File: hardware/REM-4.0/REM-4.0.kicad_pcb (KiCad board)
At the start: 2 copper layers, 98.4 x 44.5 mm, 35 parts, among them J1 Conn_01x04, J2 Conn_01x03, Q1 IRF840, U1 NE555P

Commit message: new file:   .~BoM.xlsx 	new file:   BoM.xlsx 	new file:   hardware/BoM.xlsx 	deleted:    hardware/MSD-1.0/MSD-1.0-backups/MSD-1.0-2025-03-26_092035.zip 	deleted:    hardware/MSD-1.0/MSD-1.0-backups/MSD-1.0-2025-03-26_092834.zip 	deleted:    hardware/MSD-1.0/MSD-1.0-backups/MSD-1.0-2025-03-27_092014.zip 	new file:   hardware/MSD-1.0/MSD-1.0-backups/MSD-1.0-2025-04-28_130614.zip 	new file:   hardware/MSD-1.0/MSD-1.0-backups/MSD-1.0-2025-04-28_131128.zip 	new file:   hardware/MSD-1.0/MSD-1.0-backups/MSD-1.0-2025-04-28_132753.zip 	new file:   hardware/MSD-1.0/MSD-1.0.csv 	modified:   hardware/MSD-1.0/MSD-1.0.kicad_pcb 	modified:   hardware/MSD-1.0/MSD-1.0.kicad_sch 	deleted:    hardware/PS-1.0/PS-1.0-backups/PS-1.0-2025-03-24_111800.zip 	deleted:    hardware/PS-1.0/PS-1.0-backups/PS-1.0-2025-03-24_112738.zip 	deleted:    hardware/PS-1.0/PS-1.0-backups/PS-1.0-2025-03-25_152833.zip 	deleted:    hardware/PS-1.0/PS-1.0-backups/PS-1.0-2025-03-25_154601.zip 	deleted:    hardware/PS-1.0/PS-1.0-backups/PS-1.0-2025-03-25_155821.zip 	deleted:    hardware/PS-1.0/PS-1.0-backups/PS-1.0-2025-04-11_101418.zip 	deleted:    hardware/PS-1.0/PS-1.0-backups/PS-1.0-2025-04-11_110528.zip 	deleted:    hardware/PS-1.0/PS-1.0-backups/PS-1.0-2025-04-11_111527.zip 	deleted:    hardware/PS-1.0/PS-1.0-backups/PS-1.0-2025-04-11_114252.zip 	deleted:    hardware/PS-1.0/PS-1.0-backups/PS-1.0-2025-04-17_105409.zip 	new file:   hardware/PS-1.0/PS-1.0-backups/PS-1.0-2025-04-19_071925.zip 	new file:   hardware/PS-1.0/PS-1.0-backups/PS-1.0-2025-04-27_222808.zip 	new file:   hardware/PS-1.0/PS-1.0-backups/PS-1.0-2025-04-27_223939.zip 	new file:   hardware/PS-1.0/PS-1.0-backups/PS-1.0-2025-04-27_224445.zip 	new file:   hardware/PS-1.0/PS-1.0-backups/PS-1.0-2025-04-27_225206.zip 	new file:   hardware/PS-1.0/PS-1.0-backups/PS-1.0-2025-04-27_230217.zip 	new file:   hardware/PS-1.0/PS-1.0-backups/PS-1.0-2025-04-28_083014.zip 	new file:   hardware/PS-1.0/PS-1.0-backups/PS-1.0-2025-04-28_112951.zip 	new file:   har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
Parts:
- C1: value 2.2nF -> 2.2nF 100
- C11, C12: value C -> 0.01µF 1000
- C2: value 10nF -> 10nF 63
- C3: value 0.022uF 400V MKP -> 0.022µF 400V
- C4: value 22nF -> 22nF 100
- C5, C6, C8: value 100nF -> 100nF 100
- J1: value Conn_01x04 -> PinHeader_2.54mm 02x04 Horizontal
- J2: value Conn_01x03 -> PinHeader_2.54mm 02x05 Horizontal
- R8, R9: value 33Ω -> 33Ω 2W
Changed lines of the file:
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@@
 			)
 		)
-		(property "Value" "C"
+		(property "Value" "0.01µF 1000"
 			(at 5 3.75 90)
 			(layer "F.Fab")
@@
 			)
 		)
-		(property "Value" "Conn_01x03"
+		(property "Value" "PinHeader_2.54mm 02x05 Horizontal"
 			(at 5.08 12.7 -90)
 			(unlocked yes)
@@
 			)
 		)
-		(property "Value" "2.2nF"
+		(property "Value" "2.2nF 100"
 			(at 2.5 3 0)
 			(layer "F.Fab")
@@
 			)
 		)
-		(property "Value" "Conn_01x04"
+		(property "Value" "PinHeader_2.54mm 02x04 Horizontal"
 			(at 5.08 10.16 -90)
 			(unlocked yes)
@@
 			)
 		)
-		(property "Value" "33Ω"
+		(property "Value" "33Ω 2W"
 			(at 10.16 3.37 90)
 			(layer "F.Fab")
@@
 			)
 		)
-		(property "Value" "22nF"
+		(property "Value" "22nF 100"
 			(at 2.5 3 -90)
 			(layer "F.Fab")
@@
 		(tags "test point THT pad")
 		(property "Reference" "JP7"
-			(at 0 -1.648 360)
+			(at 0 -1.648 0)
 			(layer "F.SilkS")
 			(hide yes)
@@
 		)
 		(property "Value" "TestPoint"
-			(at 0 1.75 360)
+			(at 0 1.75 0)
 			(layer "F.Fab")
 			(effects
@@
 		)
 		(fp_text user "${REFERENCE}"
-			(at 0 -1.65 360)
+			(at 0 -1.65 0)
 			(layer "F.Fab")
 			(effects
@@
 			)
 		)
-		(property "Value" "100nF"
+		(property "Value" "100nF 100"
 			(at 2.5 3 -90)
 			(layer "F.Fab")
@@
 			)
 		)
-		(property "Value" "C"
+		(property "Value" "0.01µF 1000"
 			(at 5 3.75 90)
 			(layer "F.Fab")
@@
 			)
 		)
-		(property "Value" "100nF"
+		(property "Value" "100nF 100"
 			(at 2.5 3 -90)
 			(layer "F.Fab")
@@
 			)
 		)
-		(property "Value" "0.022uF 400V MKP"
+		(property "Value" "0.022µF 400V"
 			(at 5 3.75 0)
 			(layer "F.Fab")
@@
 			)
 		)
-		(property "Value" "100nF"
+		(property "Value" "100nF 100"
 			(at 2.5 3 0)
 			(layer "F.Fab")
@@
 			)
 		)
-		(property "Value" "33Ω"
+		(property "Value" "33Ω 2W"
 			(at 10.16 3.37 90)
 			(layer "F.Fab")
@@
 			)
 		)
-		(property "Value" "10nF"
+		(property "Value" "10nF 63"
 			(at 2.5 3 0)
 			(layer "F.Fab")

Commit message: modified:   README.md 	deleted:    hardware/CTL-1.0/CTL-1.0-backups/CTL-1.0-2025-05-28_203806.zip 	deleted:    hardware/CTL-1.0/CTL-1.0-backups/CTL-1.0-2025-05-28_204313.zip 	deleted:    hardware/CTL-1.0/CTL-1.0-backups/CTL-1.0-2025-05-30_173028.zip 	deleted:    hardware/CTL-1.0/CTL-1.0-backups/CTL-1.0-2025-05-30_174116.zip 	deleted:    hardware/CTL-1.0/CTL-1.0-backups/CTL-1.0-2025-05-30_175122.zip 	new file:   hardware/CTL-1.0/CTL-1.0-backups/CTL-1.0-2025-07-24_151142.zip 	new file:   hardware/CTL-1.0/CTL-1.0-backups/CTL-1.0-2025-07-24_172002.zip 	new file:   hardware/CTL-1.0/CTL-1.0-backups/CTL-1.0-2025-07-25_175122.zip 	new file:   hardware/CTL-1.0/CTL-1.0-backups/CTL-1.0-2025-07-26_120011.zip 	new file:   hardware/CTL-1.0/CTL-1.0-backups/CTL-1.0-2025-07-26_120808.zip 	modified:   hardware/CTL-1.0/CTL-1.0.kicad_pcb 	modified:   hardware/CTL-1.0/CTL-1.0.kicad_pro 	new file:   hardware/CTL-1.0/CTL-1.0.step 	deleted:    hardware/MSD-1.0/MSD-1.0-backups/MSD-1.0-2025-04-11_111943.zip 	deleted:    hardware/MSD-1.0/MSD-1.0-backups/MSD-1.0-2025-04-11_113401.zip 	new file:   hardware/MSD-1.0/MSD-1.0-backups/MSD-1.0-2025-07-25_163151.zip 	new file:   hardware/MSD-1.0/MSD-1.0-backups/MSD-1.0-2025-07-25_171843.zip 	modified:   hardware/MSD-1.0/MSD-1.0.kicad_pcb 	modified:   hardware/MSD-1.0/MSD-1.0.step 	new file:   hardware/MSD-1.1/MSD-1.1-backups/MSD-1.1-2025-07-24_151252.zip 	new file:   hardware/MSD-1.1/MSD-1.1-backups/MSD-1.1-2025-07-25_152939.zip 	new file:   hardware/MSD-1.1/MSD-1.1-backups/MSD-1.1-2025-07-25_162346.zip 	new file:   hardware/MSD-1.1/MSD-1.1-backups/MSD-1.1-2025-07-25_162917.zip 	modified:   hardware/MSD-1.1/MSD-1.1.kicad_pcb 	modified:   hardware/MSD-1.1/MSD-1.1.step 	modified:   hardware/MSD-1.1/fp-info-cache 	new file:   hardware/MSD-2.0/MSD-2.0-backups/MSD-2.0-2025-07-24_151230.zip 	deleted:    hardware/PS-2.0/PS-2.0-backups/PS-2.0-2025-05-07_010425.zip 	deleted:    hardware/PS-2.0/PS-2.0-backups/PS-2.0-2025-05-09_084820.zip 	deleted:    hardware/P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
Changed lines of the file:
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@@
 			(unlocked yes)
 			(layer "F.Fab")
-			(hide yes)
 			(effects
 				(font
@@
 			(end 0 -11.684)
 			(stroke
-				(width 0.1)
+				(width 0.15)
 				(type default)
 			)
@@
 			(end 0 -7.112)
 			(stroke
-				(width 0.1)
+				(width 0.15)
 				(type default)
 			)
@@
 		)
 		(pad "1" thru_hole circle
-			(at -7.62 -10.16 90)
+			(at -5.08 -11.43 90)
 			(size 3 3)
 			(drill 1.5)
@@
 		)
 		(pad "2" thru_hole circle
-			(at -2.54 5.08 90)
+			(at -1.27 5.715 90)
 			(size 3 3)
 			(drill 1.5)
@@
 			(pintype "passive")
 		)
+		(model "/Users/margabudi/Documents/KiCad/8.0/3dmodels/Transformer/XF_Toroid_OD20_ID14_H08.step"
+			(offset
+				(xyz 0 0 0)
+			)
+			(scale
+				(xyz 1 1 1)
+			)
+			(rotate
+				(xyz 0 0 0)
+			)
+		)
 	)

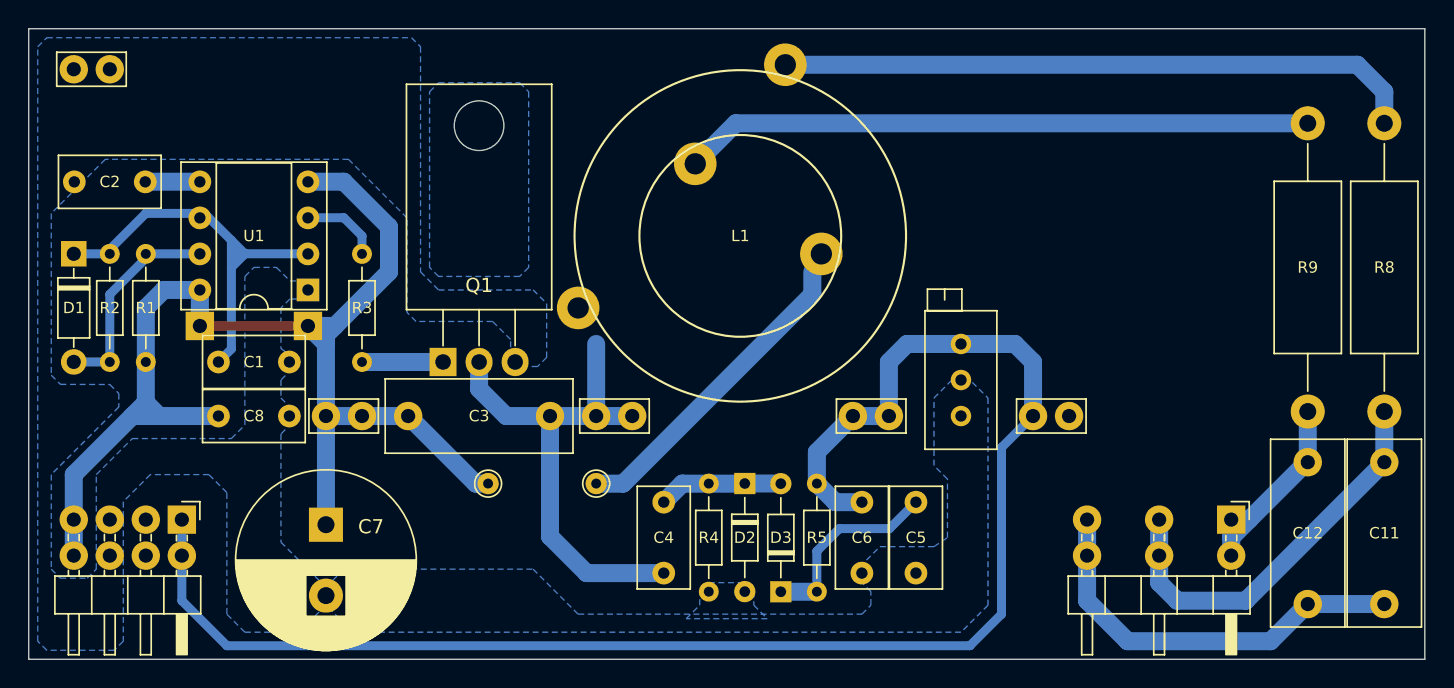
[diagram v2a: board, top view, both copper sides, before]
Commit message: modified:   .DS_Store 	new file:   CAD/FR_TEST.dxf 	modified:   Ferrite Transformer Calculation.xlsx 	new file:   archive/PR_ 0201_2026.docx 	modified:   archive/Purchase 20260105.xlsx 	new file:   archive/Purchase 20260209.zip 	new file:   archive/Purchase 20260209/Invoice | Tokopedia 1.pdf 	new file:   archive/Purchase 20260209/Invoice | Tokopedia 2.pdf 	new file:   archive/Purchase 20260209/Invoice | Tokopedia 3.pdf 	new file:   archive/Purchase 20260209/Invoice | Tokopedia 4.pdf 	new file:   archive/Purchase 20260209/Invoice | Tokopedia 5.pdf 	new file:   archive/Purchase_20260109_0924.jpg 	new file:   archive/Purchase_20260209_0924.xlsx 	new file:   archive/R parallel.xlsx 	modified:   firmware/ESP32-S3 PWM/include/config.h 	modified:   firmware/ESP32-S3 PWM/include/hardware_control.h 	modified:   firmware/ESP32-S3 PWM/platformio.ini 	modified:   firmware/ESP32-S3 PWM/src/hardware_control.cpp 	modified:   firmware/ESP32-S3 PWM/src/main.cpp 	new file:   hardware/CTL-4.3/CTL-4.3-backups/CTL-4.3-2026-02-11_163805.zip 	new file:   hardware/CTL-4.3/CTL-4.3-backups/CTL-4.3-2026-02-13_145455.zip 	new file:   hardware/CTL-4.3/CTL-4.3-backups/CTL-4.3-2026-02-13_163249.zip 	new file:   hardware/CTL-4.3/CTL-4.3-backups/CTL-4.3-2026-02-18_163417.zip 	new file:   hardware/CTL-4.3/CTL-4.3-backups/CTL-4.3-2026-02-19_083102.zip 	new file:   hardware/CTL-4.3/CTL-4.3-backups/CTL-4.3-2026-03-04_102408.zip 	modified:   hardware/CTL-4.3/fp-info-cache 	new file:   hardware/CTL-5.0/CTL-4.3-backups/CTL-4.3-2026-01-19_105947.zip 	new file:   hardware/CTL-5.0/CTL-4.3-backups/CTL-4.3-2026-01-19_110601.zip 	new file:   hardware/CTL-5.0/CTL-4.3-backups/CTL-4.3-2026-01-19_111804.zip 	new file:   hardware/CTL-5.0/CTL-4.3-backups/CTL-4.3-2026-01-19_113721.zip 	new file:   hardware/CTL-5.0/CTL-4.3-backups/CTL-4.3-2026-01-19_164107.zip 	new file:   hardware/CTL-5.0/CTL-4.3-backups/CTL-4.3-2026-01-20_112913.zip 	new file:   hardware/CTL-5.0/CTL-4.3-backups/CTL-4.3-2026-02-11_163805.zip 	new file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
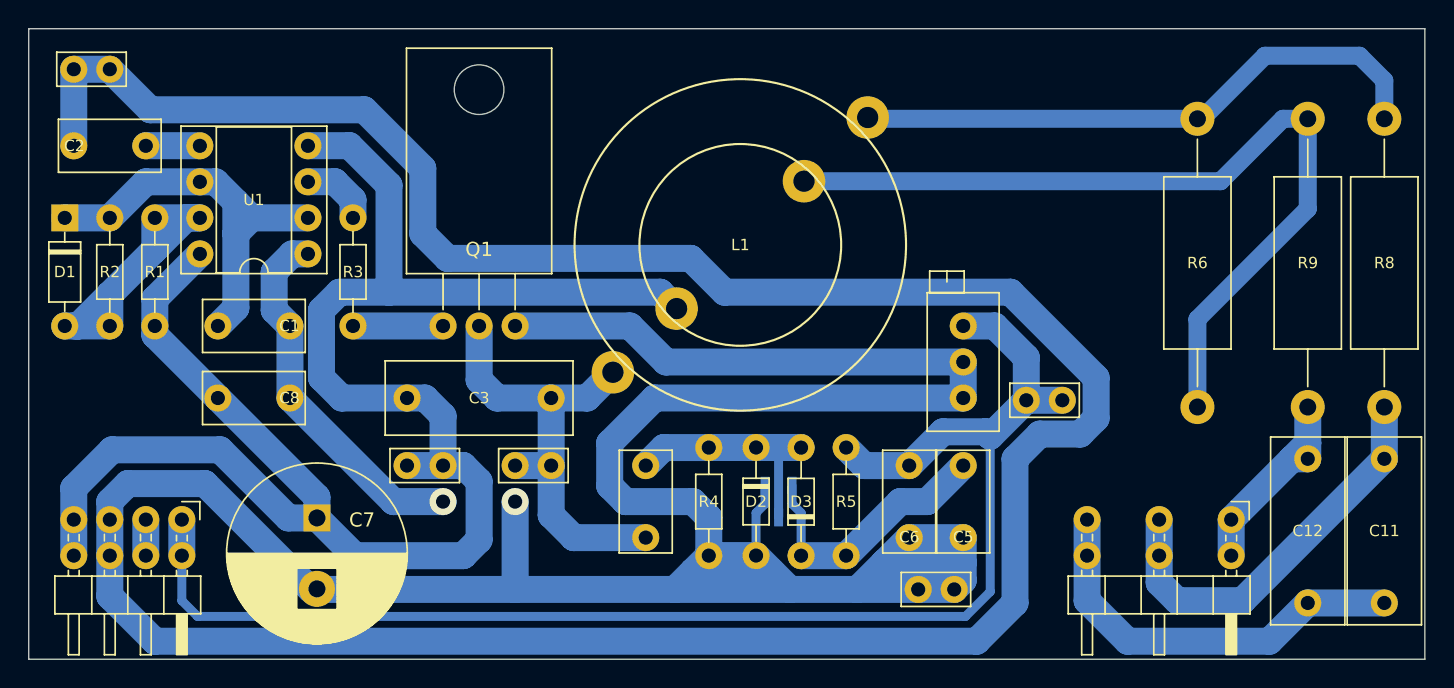
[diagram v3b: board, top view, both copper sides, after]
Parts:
- removed JP1, JP2: TestPoint, TestPoint:TestPoint_THTPad_2.0x2.0mm_Drill1.0mm_NoSilkscreen
- removed JP7, JP8: TestPoint, TestPoint:TestPoint_THTPad_D1.5mm_Drill0.7mm
- removed TP6: ~, TestPoint:TestPoint_Bridge_Pitch2.54mm_Drill1.0mm
- added D4: BAT54S, Package_TO_SOT_SMD:SOT-23, B.Cu at (148.1, 100.0)
- added R6: 120Ω 2W, Resistor_THT:R_Axial_DIN0414_L11.9mm_D4.5mm_P20.32mm_Horizontal, F.Cu at (177.6, 73.0)
- added TP3: ~, TestPoint:TestPoint_Bridge_Pitch2.54mm_Drill1.0mm, F.Cu at (158.0, 106.2)
- D2, D3: value 1N4148 -> BAT85
- Q1: value IRF840 -> IRLB3034PbF
- RV1: value 1kΩ -> 5kΩ
- moved TP5 12.3 mm to (168.1, 92.9)
- moved TP1 6.70 mm to (121.9, 97.5)
- moved TP2 6.70 mm to (132.1, 97.5)
- moved C3 5.16 mm to (127.0, 92.7)
- moved C11 4.84 mm to (190.8, 102.1)
- moved C12 4.84 mm to (185.4, 102.1)
- moved C1 3.56 mm to (111.1, 87.6)
- moved C2 3.56 mm to (101.0, 74.9)
- moved C5 3.33 mm to (161.1, 100.0)
- moved C6 3.33 mm to (157.3, 100.0)
- moved R5 3.27 mm to (152.9, 100.0)
- moved D3 2.91 mm to (149.7, 103.8)
- moved C8 2.80 mm to (111.1, 92.7)
- moved D2 2.66 mm to (146.5, 96.2)
- moved R1 2.62 mm to (104.1, 83.8)
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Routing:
- net GND: track 0.00 -> 386.2 mm, vias 0 -> 2
- net +5V: track 112.9 -> 130.7 mm
- net Net-(L1-Pad3): track 44.4 -> 60.9 mm
- net Net-(J1-Pin_1): track 111.5 -> 101.3 mm
- net Net-(D1-A): track 14.7 -> 22.5 mm
- net Net-(D2-K): track 8.80 -> 16.4 mm
- net Net-(D3-K): track 13.8 -> 19.3 mm
- net Net-(Q1-D): track 36.1 -> 32.6 mm
- net Net-(L1-Pad4): track 45.2 -> 42.0 mm
- net unconnected-(J1-Pin_2-Pad2): track 0.00 -> 2.54 mm
- net Net-(Q1-G): track 5.71 -> 6.35 mm
- net Net-(U1-Q): track 5.62 -> 4.99 mm
- removed copper zone on B.Cu, net (none)
- removed copper zone on B.Cu, net GND
